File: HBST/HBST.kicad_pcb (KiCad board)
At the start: 4 copper layers, 100 x 100 mm, 15 parts, among them J1 Conn_01x06_Pin, J3 Conn_01x04_Pin, J4 Conn_01x13_Pin, J5 Conn_01x09_Pin

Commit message: updated design
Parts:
- added R3: 50, Resistor_SMD:R_0805_2012Metric_Pad1.20x1.40mm_HandSolder, F.Cu at (150.9, 89.3)
- added R4: 50, Resistor_SMD:R_0805_2012Metric_Pad1.20x1.40mm_HandSolder, F.Cu at (153.9, 89.3)
- added TP3: TestPoint_Small, TestPoint:TestPoint_Pad_D1.0mm, F.Cu at (151.0, 93.8)
- added TP4: TestPoint_Small, TestPoint:TestPoint_Pad_D1.0mm, F.Cu at (153.9, 93.8)
- moved R2 7.45 mm to (148.1, 89.3), turned to 90 degrees
- moved R1 4.34 mm to (145.0, 89.3), turned to 90 degrees
- moved TP1 3.55 mm to (145.0, 93.8), turned to 0 degrees
- moved TP2 2.75 mm to (148.1, 93.8), turned to 180 degrees
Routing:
- net Net-(R3-Pad1): track 0.00 -> 3.62 mm
- net Net-(R4-Pad1): track 0.00 -> 3.50 mm
- net Net-(R2-Pad1): track 2.30 -> 3.70 mm
- net Net-(R1-Pad1): track 2.15 -> 3.55 mm

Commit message: added decoupling capacitors and fixed copper fill zone on In2 copper layer
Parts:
- added C1: 10nF, Capacitor_SMD:C_0805_2012Metric, F.Cu at (142.0, 93.8)
- added C10: 0.1uF, Capacitor_SMD:C_0805_2012Metric, F.Cu at (165.2, 97.2)
- added C11: 1uF, Capacitor_SMD:C_0805_2012Metric, F.Cu at (156.8, 106.1)
- added C12: 10uF, Capacitor_SMD:C_0805_2012Metric, F.Cu at (156.8, 104.1)
- added C13: 10nF, Capacitor_SMD:C_0805_2012Metric, F.Cu at (139.8, 89.2)
- added C14: 0.1uF, Capacitor_SMD:C_0805_2012Metric, F.Cu at (141.8, 89.2)
- added C15: 1uF, Capacitor_SMD:C_0805_2012Metric, F.Cu at (157.9, 89.2)
- added C16: 10uF, Capacitor_SMD:C_0805_2012Metric, F.Cu at (159.9, 89.2)
- added C2: 0.1uF, Capacitor_SMD:C_0805_2012Metric, F.Cu at (142.0, 95.8)
- added C3: 1uF, Capacitor_SMD:C_0805_2012Metric, F.Cu at (142.1, 102.9)
- added C4: 10uF, Capacitor_SMD:C_0805_2012Metric, F.Cu at (142.2, 104.9)
- added C5: 10nF, Capacitor_SMD:C_0805_2012Metric, F.Cu at (143.9, 107.7)
- added C6: 0.1uF, Capacitor_SMD:C_0805_2012Metric, F.Cu at (145.9, 107.7)
- added C7: 1uF, Capacitor_SMD:C_0805_2012Metric, F.Cu at (153.7, 107.8)
- added C8: 10uF, Capacitor_SMD:C_0805_2012Metric, F.Cu at (151.7, 107.8)
- added C9: 10nF, Capacitor_SMD:C_0805_2012Metric, F.Cu at (158.1, 93.2)
- added J2: Conn_01x02, Connector_PinHeader_2.54mm:PinHeader_1x02_P2.54mm_Horizontal, F.Cu at (110.2, 121.9)
- added J6: Conn_01x02, Connector_PinHeader_2.54mm:PinHeader_1x02_P2.54mm_Horizontal, F.Cu at (139.7, 138.9)
- added J7: Conn_01x02, Connector_PinHeader_2.54mm:PinHeader_1x02_P2.54mm_Horizontal, F.Cu at (188.9, 70.4)
- added J8: Conn_01x02, Connector_PinHeader_2.54mm:PinHeader_1x02_P2.54mm_Horizontal, F.Cu at (175.3, 138.9)
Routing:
- net VDD: track 0.00 -> 32.4 mm, vias 0 -> 8
- net GND: track 1.23 -> 3.29 mm
- added copper zone on In2.Cu, net VDD

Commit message: minor update
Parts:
- moved J2 2.20 mm to (110.1, 124.1)
- moved J6 0.33 mm to (140.0, 138.9)
- moved TP2 0.10 mm to (148.0, 93.8)
- moved TP4 0.10 mm to (154.0, 93.8)
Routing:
- net GND: track 3.29 -> 1.23 mm
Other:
- board text added: "GND VDD"
- board text added: "VDD GND"
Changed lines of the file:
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@@
 	(footprint "TestPoint:TestPoint_Pad_D1.0mm"
 		(layer "F.Cu")
-		(at 148.1 93.8 180)
+		(at 148 93.8 180)
 		(descr "SMD pad as test Point, diameter 1.0mm")
 		(tags "test point SMD pad")
@@
 	(footprint "Connector_PinHeader_2.54mm:PinHeader_1x02_P2.54mm_Horizontal"
 		(layer "F.Cu")
-		(at 110.2 121.94 180)
+		(at 110.1 124.14 180)
 		(descr "Through hole angled pin header, 1x02, 2.54mm pitch, 6mm pin length, single row")
 		(tags "Through hole angled pin header THT 1x02 2.54mm single row")
@@
 		(tags "capacitor")
 		(property "Reference" "C3"
-			(at -2.85 0 0)
+			(at -2.7 0 0)
 			(layer "F.SilkS")
 			(effects
@@
 	(footprint "Connector_PinHeader_2.54mm:PinHeader_1x02_P2.54mm_Horizontal"
 		(layer "F.Cu")
-		(at 188.9 70.36)
+		(at 188.925 70.36)
 		(descr "Through hole angled pin header, 1x02, 2.54mm pitch, 6mm pin length, single row")
 		(tags "Through hole angled pin header THT 1x02 2.54mm single row")
@@
 	(footprint "TestPoint:TestPoint_Pad_D1.0mm"
 		(layer "F.Cu")
-		(at 153.9 93.8 90)
+		(at 154 93.8 90)
 		(descr "SMD pad as test Point, diameter 1.0mm")
 		(tags "test point SMD pad")
@@
 		(tags "capacitor")
 		(property "Reference" "C4"
-			(at -2.6 0.1 0)
+			(at -2.75 0.1 0)
 			(layer "F.SilkS")
 			(effects
@@
 	(footprint "Connector_PinHeader_2.54mm:PinHeader_1x02_P2.54mm_Horizontal"
 		(layer "F.Cu")
-		(at 139.675 138.925 -90)
+		(at 140 138.9 -90)
 		(descr "Through hole angled pin header, 1x02, 2.54mm pitch, 6mm pin length, single row")
 		(tags "Through hole angled pin header THT 1x02 2.54mm single row")
@@
 	)
 	(gr_text "T_SAMPLE\nT_SDOUT\nT_CK_SHIFT\nT_EN_SHIFT\nT_CK2\nT_RST_N\nT_CK1\nT_AVDD\nGND"
-		(at 187.5 123.6 0)
+		(at 187 123.4 0)
 		(layer "F.SilkS")
 		(effects
@@
 		)
 	)
+	(gr_text "VDD\nGND"
+		(at 182.2 73.9 0)
+		(layer "F.SilkS")
+		(effects
+			(font
+				(size 1.6 1.5)
+				(thickness 0.3)
+				(bold yes)
+			)
+			(justify left bottom)
+		)
+	)
 	(gr_text "Sanderling"
 		(at 101.6 79.95 0)
@@
 		)
 	)
+	(gr_text "GND\nVDD"
+		(at 112 125.1 0)
+		(layer "F.SilkS")
+		(effects
+			(font
+				(size 1.6 1.5)
+				(thickness 0.3)
+				(bold yes)
+			)
+			(justify left bottom)
+		)
+	)
 	(gr_text "GND\nS_DC2_Vvar2_b\nS_DC2_Vvar2_sd\nS_DC2_Vvar1_sd\nS_DC2_Vvar1_b\nS_HC_Vvar1_b\nS_HC_Vvar1_sd\nS_HC_Vvar2_sd\nS_HC_Vvar2_b\nS_DC1_Vvar1_b\nS_DC1_Vvar1_sd\nS_DC1_Vvar2_sd\nS_DC1_Vvar2_b"
 		(at 111.95 114.15 0)
@@
 		)
 	)
-	(segment
-		(start 149.7 95.55)
-		(end 149.7 96.1)
-		(width 0.1)
-		(layer "F.Cu")
-		(net 1)
-	)
-	(segment
-		(start 146.5 95.55)
-		(end 146.5 96.5)
-		(width 0.1)
-		(layer "F.Cu")
-		(net 1)
+	(gr_text "GND\nVDD"
+		(at 141.1 136.9 90)
+		(layer "F.SilkS")
+		(effects
+			(font
+				(size 1.6 1.5)
+				(thickness 0.3)
+				(bold yes)
+			)
+			(justify left bottom)
+		)
 	)
 	(segment
@@
 		(layer "F.Cu")
 		(net 1)
-	)
-	(segment
-		(start 149.7 96.1)
-		(end 150.1 96.5)
-		(width 0.1)
-		(layer "F.Cu")
-		(net 1)

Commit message: added description
Signed-off-by: Habibur Rahman <accounts@emon.no>
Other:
- board text added: "University of Oslo Department of Informatics V1RevA 27 Sep 2024"
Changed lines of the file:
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@@
 	)
 	(gr_text "Bananaquit"
-		(at 143 125.55 0)
+		(at 142.3 125.1 0)
 		(layer "F.SilkS")
 		(effects
@@
 				(thickness 0.3)
 				(bold yes)
+			)
+			(justify left bottom)
+		)
+	)
+	(gr_text "University of Oslo\nDepartment of Informatics\nV1RevA 27 Sep 2024 \n"
+		(at 138.8 72.3 0)
+		(layer "F.SilkS")
+		(effects
+			(font
+				(size 1.5 1.5)
+				(thickness 0.3)
+				(bold yes)

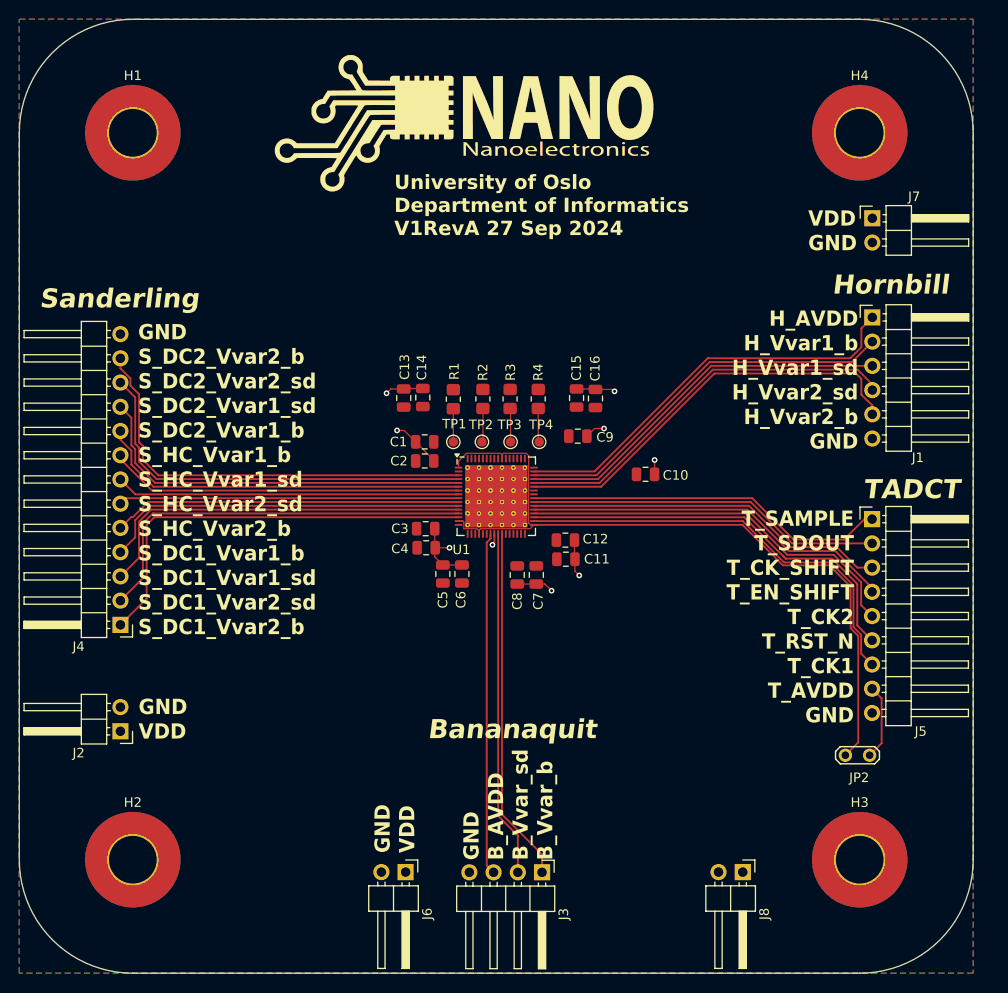
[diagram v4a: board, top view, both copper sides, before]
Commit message: fixed to correct package and minor component placement changes
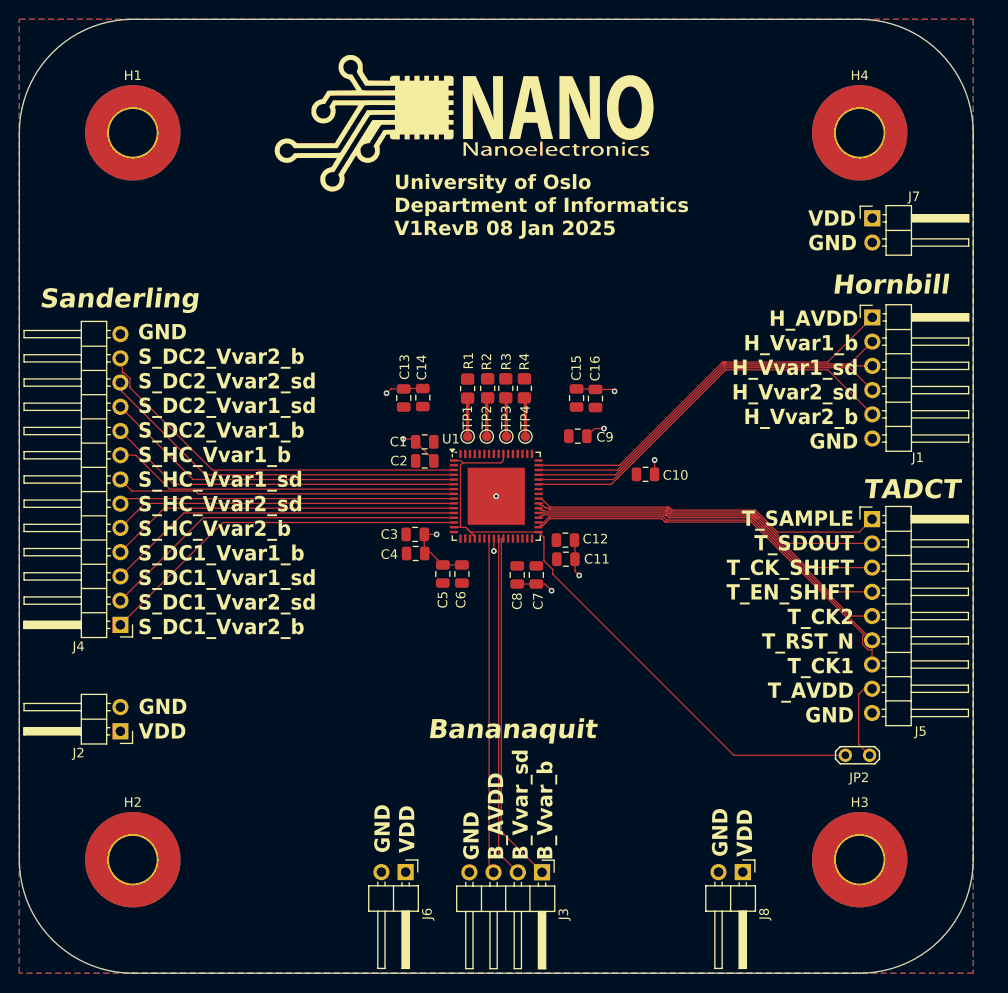
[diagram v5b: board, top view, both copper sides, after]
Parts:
- U1: footprint Package_DFN_QFN:QFN-64-1EP_8x8mm_P0.4mm_EP6.5x6.5mm_ThermalVias -> Package_DFN_QFN:QFN-64-1EP_9x9mm_P0.5mm_EP6x6mm
- moved R1 1.87 mm to (146.5, 88.2)
- moved R4 1.83 mm to (152.4, 88.2)
- moved TP1 1.60 mm to (146.5, 93.2)
- moved TP4 1.56 mm to (152.6, 93.2)
- moved C3 1.25 mm to (141.0, 103.5)
- moved C4 1.25 mm to (141.1, 105.5)
- moved R2 1.22 mm to (148.6, 88.2)
- moved R3 1.20 mm to (150.5, 88.2)
- moved TP2 0.75 mm to (148.5, 93.2)
- moved TP3 0.72 mm to (150.6, 93.2)
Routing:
- net Net-(JP2-A): track 80.8 -> 66.9 mm
- net /S_DC1_Vvar2_b: track 44.7 -> 39.2 mm
- net /S_DC2_Vvar2_b: track 45.4 -> 41.2 mm
- net /S_DC1_Vvar2_sd: track 42.6 -> 38.6 mm
- net /S_DC2_Vvar2_sd: track 43.3 -> 39.6 mm
- net /S_DC2_Vvar1_sd: track 41.3 -> 38.1 mm
- net /S_DC1_Vvar1_sd: track 40.6 -> 37.7 mm
- net /T_RST_N: track 43.4 -> 40.6 mm
- net /T_CK1: track 45.4 -> 43.4 mm
- net /S_DC2_Vvar1_b: track 39.3 -> 37.3 mm
- net /H_AVDD: track 43.3 -> 41.4 mm
- net /T_CK2: track 41.3 -> 39.5 mm
- net /H_Vvar2_b: track 43.7 -> 42.0 mm
- net /S_DC1_Vvar1_b: track 38.5 -> 36.9 mm
- net VDD: track 32.4 -> 31.0 mm
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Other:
- copper layers 4 -> 13
- board text added: "University of Oslo Department of Informatics V1RevB 08 Jan 2025"
- board text removed: "University of Oslo Department of Informatics V1RevA 27 Sep 2024"
